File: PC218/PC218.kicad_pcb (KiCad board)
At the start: 2 copper layers, 107 x 38 mm, 106 parts, among them J1 PC218_BoardEdge_44pin, Q1 BC848W, Q10 BC848W, Q11 BC848W, Q12 BC848W, Q13 BC848W, Q14 BC848W, Q15 BC848W, Q16 BC848W, Q17 BC848W, Q18 BC848W, Q19 BC848W, Q2 BC848W, Q20 BC848W, Q21 BC848W, Q22 BC848W, Q23 BC848W, Q24 BC848W, Q25 BC848W, Q26 BC848W, Q27 BC848W, Q28 BC848W, Q29 BC848W, Q3 BC848W, Q30 BC848W, Q31 BC848W, Q32 BC848W, Q33 BC848W, Q34 BC848W, Q35 BC848W, Q36 BC848W, Q37 BC848W, Q38 BC848W, Q39 BC848W, Q4 BC848W, Q40 BC848W, Q41 BC848W, Q42 BC848W, Q43 BC848W, Q44 BC848W, Q45 BC848W, Q5 BC848W, Q6 BC848W, Q7 BC848W, Q8 BC848W, Q9 BC848W

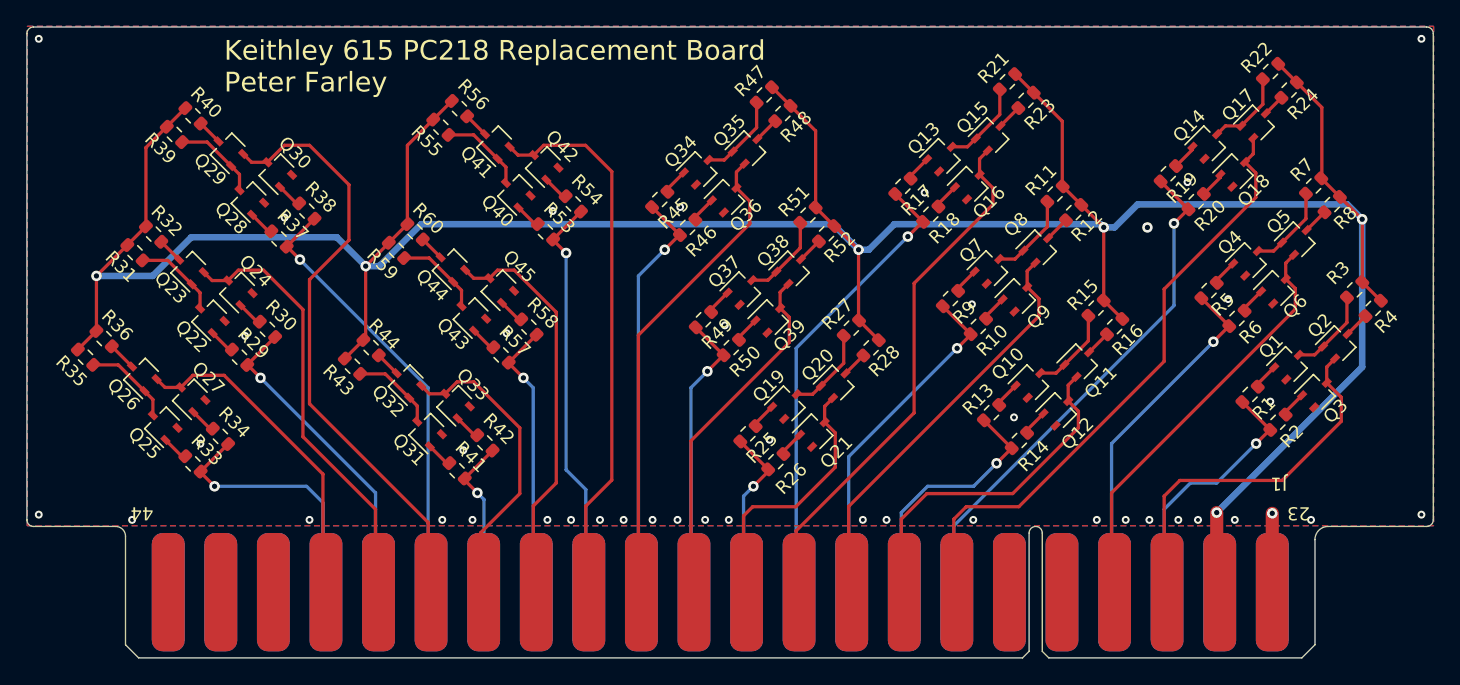
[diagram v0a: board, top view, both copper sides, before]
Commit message: PC218 Rev 1.1
Fixed disconnected ground plane resulting in two buffers being unpowered
Moved silkscreen to front, add OSHW logo
Move symbols and footprints to shared library
Update edge connector footprint to use a more sane orientation
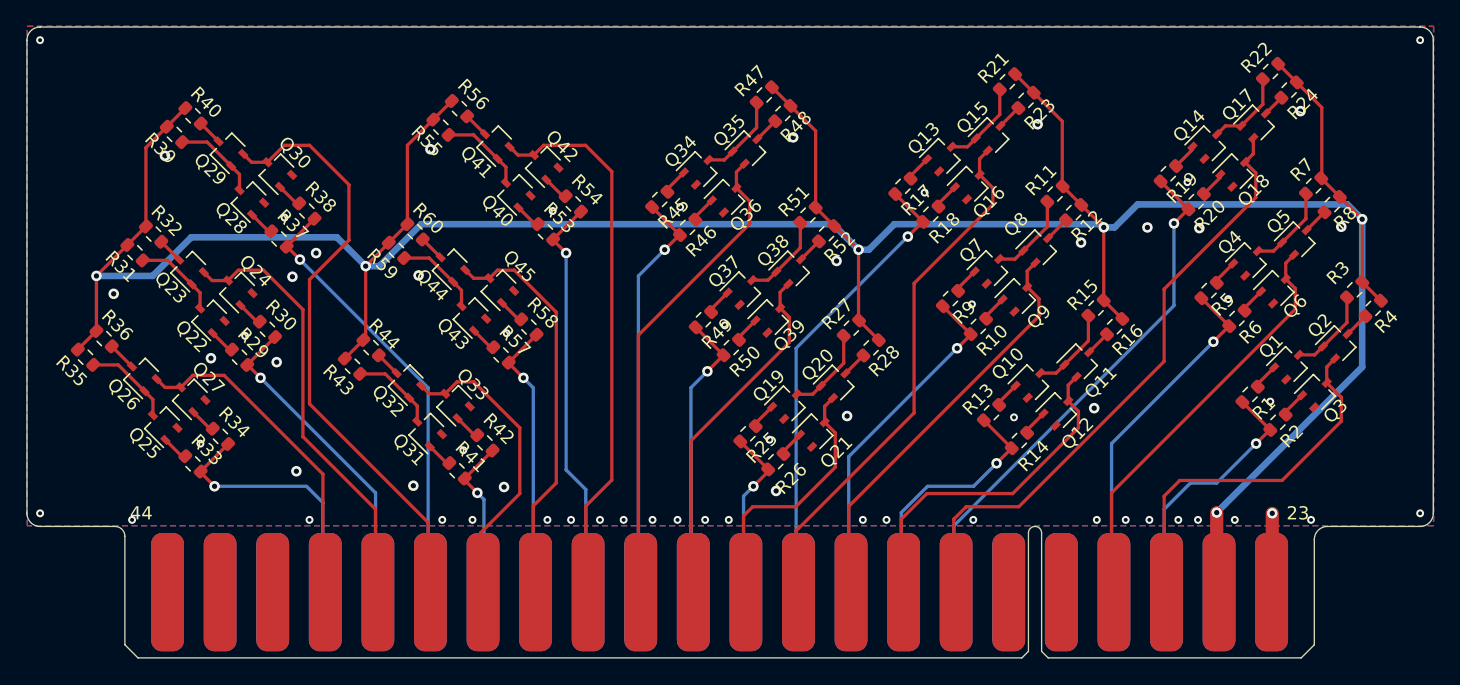
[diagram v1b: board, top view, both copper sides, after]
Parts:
- added REF**: OSHW-Logo_11.4x12mm_SilkScreen, Symbol:OSHW-Logo_11.4x12mm_SilkScreen, B.Cu at (56.4, 47.8)
- J1: footprint keithley_615_part_library:PC218_Edge_Connector -> footprints:PC218_Edge_Connector
- moved J1 91.3 mm to (55.7, 78.0), turned to 0 degrees
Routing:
- net GND: vias 43 -> 64
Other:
- outline, holes or cut-outs redrawn
- board text added: "Keithley 615 PC218 Replacement V1.1 Peter Farley, 2023"
- board text removed: "Keithley 615 PC218 Replacement Board Peter Farley"
